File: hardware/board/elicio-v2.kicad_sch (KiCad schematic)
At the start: 65 parts, among them J1 TYPE-C-31-M-14, J2 SM02B-SRSS-TB, J3 HDR-3-RA, J4 TC2030-NL, P1 SIG1, P2 SIG2, P3 REF, Q1 AO3401A, Q2 2N7002, Q3 2N7002, Q4 2N7002, Q5 2N7002, SW1 4.5x4.5x1.6, U1 MDBT50Q-1MV2, U2 ADS1292IRSMT, U3 BQ25100YFPR, U4 TLV71330PDBVR, U5 USBLC6-2SC6

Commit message: board(v2): flex layout for interface II from WP11 winner
WP11 closed interface I at 0 runs, so the board is the 2-layer flex with ring-pad tabs on A_501015_series_w20.

Co-authored-by: Cursor <cursoragent@cursor.com>
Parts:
- P1, P2, P3: footprint elicio:PAD_8x8_ENIG -> elicio:RING_PAD_D5_H2.7
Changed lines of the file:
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@@
 		(date "2026-09-17")
 		(rev "0")
-		(comment 1 "WP12 board v2. Provisional 17 x 33 mm outline. Not for order.")
+		(comment 1 "WP12 board v2. Interface II flex, packing A_501015_series_w20. Schematic contract unchanged. Not for order.")
 	)
 	(symbol
@@
 			)
 		)
-		(property "Footprint" "elicio:PAD_8x8_ENIG"
+		(property "Footprint" "elicio:RING_PAD_D5_H2.7"
 			(at 254.0 50.8 0)
 			(show_name no)
@@
 			)
 		)
-		(property "Footprint" "elicio:PAD_8x8_ENIG"
+		(property "Footprint" "elicio:RING_PAD_D5_H2.7"
 			(at 254.0 76.2 0)
 			(show_name no)
@@
 			)
 		)
-		(property "Footprint" "elicio:PAD_8x8_ENIG"
+		(property "Footprint" "elicio:RING_PAD_D5_H2.7"
 			(at 254.0 101.6 0)
 			(show_name no)

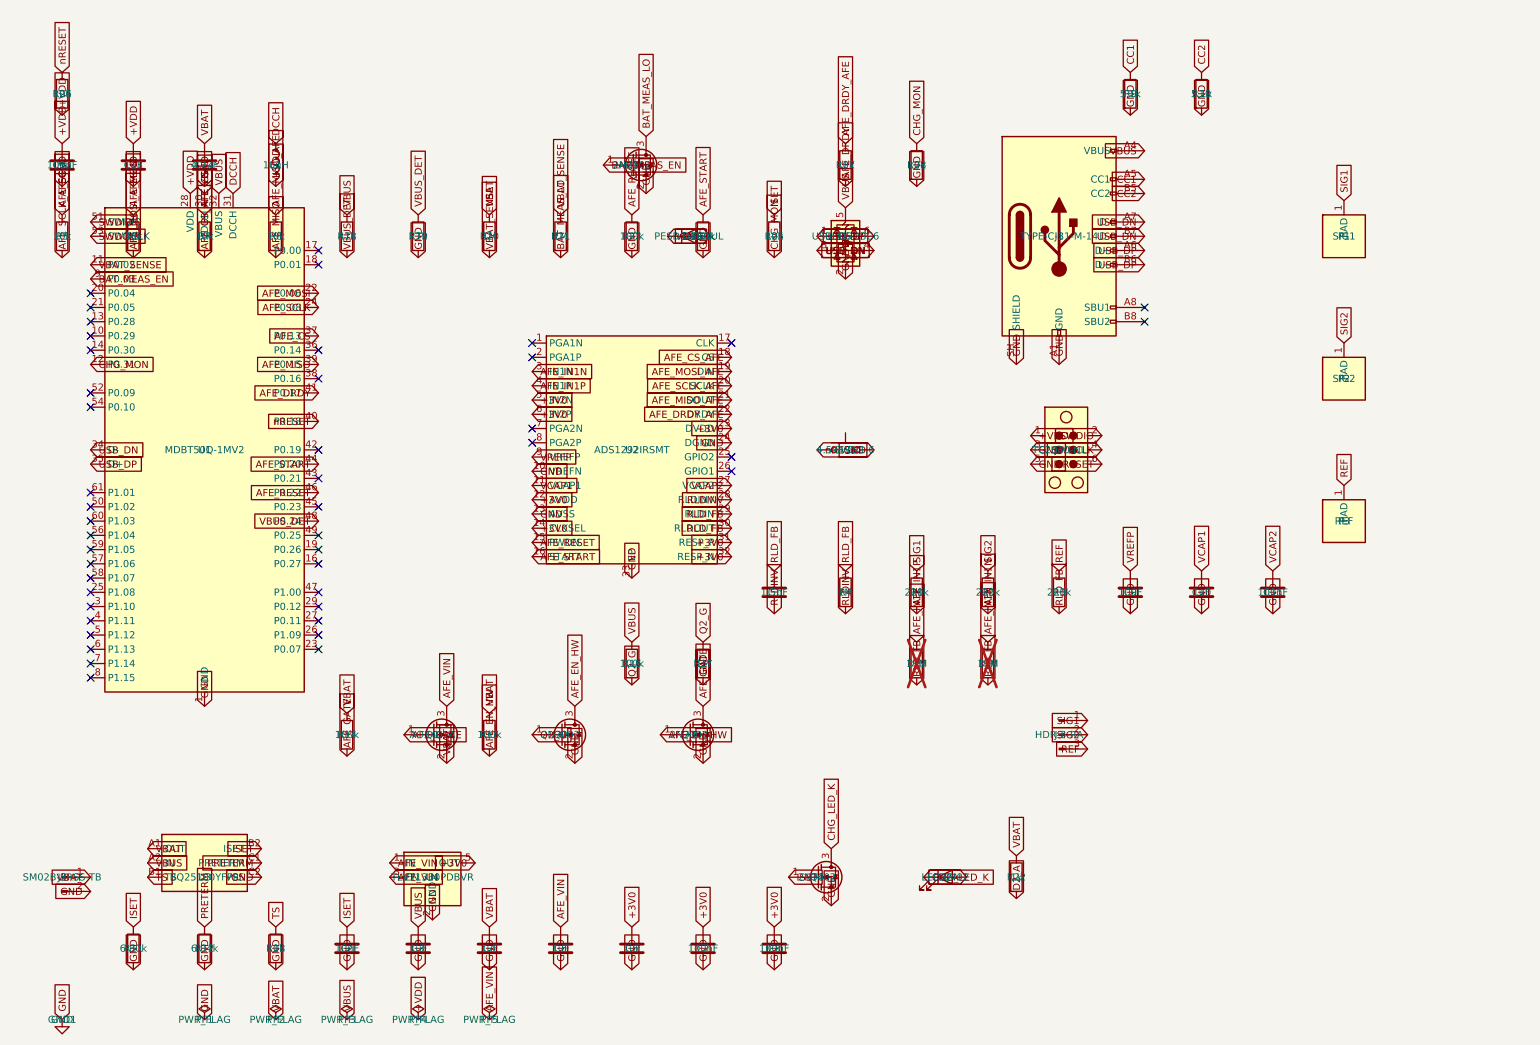
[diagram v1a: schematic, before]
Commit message: review(WP12): ISET, LED, divider, ERC 0/0, RF keep-out, routed flag, record
- ISET: R25 + R28 (20 k to GND) sat in parallel with RISET 6.80 k, so
  IOUT was about 26.6 mA, not 19.85. R28 now pulls LED_EN down; R25 alone
  feeds the high-impedance AIN7.
- LED: Q4's gate moves from ISET (about 1 V) to LED_EN (P0.04, pin 20);
  anode from VBUS, not VBAT, so it no longer loads the charger output.
- Battery divider: R21 to GND, Q5 DNP. The low-side switch left P0.02 at
  VBAT through 1 MΩ when off, above VDD + 0.3.
- ERC 0 errors, 0 warnings: mismatched symbols moved into lib/elicio as
  their embedded copies (netlist unchanged); J3 footprint library name.
- PCB: removed the length-along-s RF rule area that covered 15 module
  pads; the u-end area stays. Q5 DNP. Stiffener note 0.4.
- LCSC: C25803, C25765 and C1525 were each on two values (R1-R3 220 k
  among them); those 18 lines are blank, UNVERIFIED, for G3.
- release.py: summary has routed, tracks, nets and pads without a net;
  --routed fails closed on DRC errors, unconnected items, netless pads or
  no tracks. STEP with models. Tests cover both.
- board-v2.md: G2 default-state sentence, ESD actually used, REGOUT0 and
  the probe at a 1.8/3.0 V target, standoff stack 4.81 (no nut), foam 0.5,
  I = 0/720, decoupling deviates, DRC truth (PCB not synced, not placed).

Co-Authored-By: Claude Opus 5 <noreply@anthropic.com>
Claude-Session: https://claude.ai/code/session_014BkJUsEH26eSo9ULozTgDM
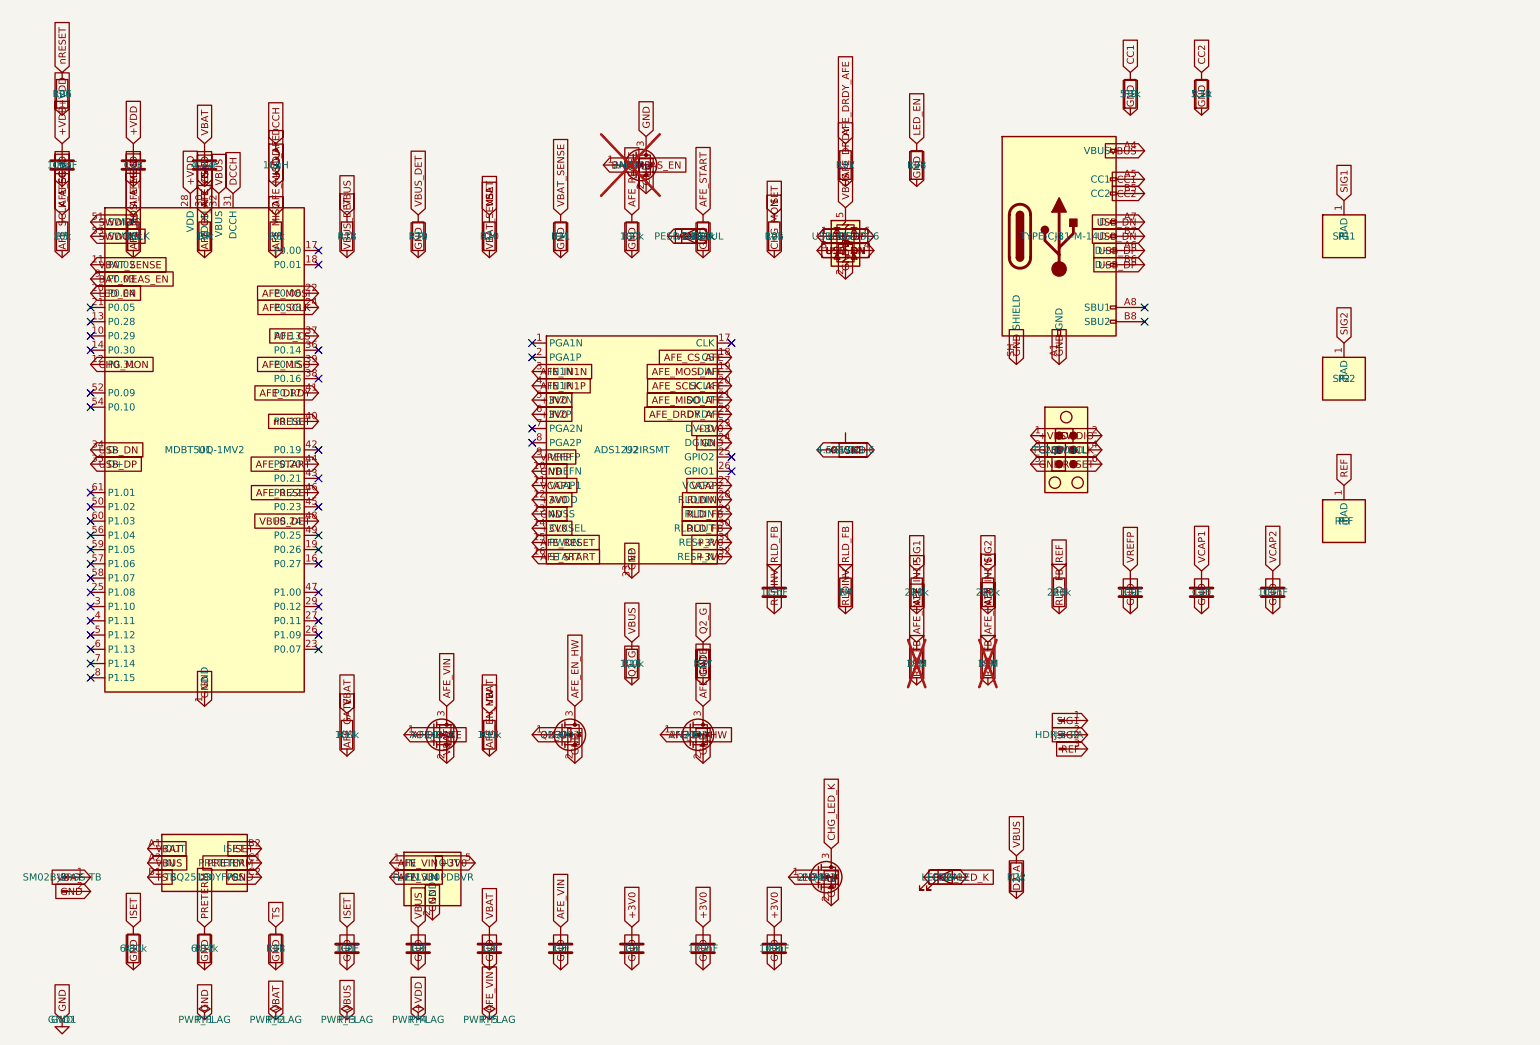
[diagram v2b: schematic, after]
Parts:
- C11, C12, C2, C7, C8: LCSC C1525 -> (none)
- D1: symbol Diode:PESD5V0L1UL -> elicio:PESD5V0L1UL
- J3: footprint Connector_PinHeader_2.54:PinHeader_1x03_P2.54mm_Horizontal -> Connector_PinHeader_2.54mm:PinHeader_1x03_P2.54mm_Horizontal
- Q1: symbol Transistor_FET:AO3401A -> elicio:AO3401A
- Q2, Q3, Q4: symbol Transistor_FET:2N7002 -> elicio:2N7002
- Q5: symbol Transistor_FET:2N7002 -> elicio:2N7002; now not fitted
- R1, R14, R15, R16, R2, R23, R24, R3: LCSC C25803 -> (none)
- R17, R20, R21, R22, R4: LCSC C25765 -> (none)
- U4: symbol Regulator_Linear:TLV71330PDBV -> elicio:TLV71330PDBV
- U5: symbol Power_Protection:USBLC6-2SC6 -> elicio:USBLC6-2SC6
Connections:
- net BAT_MEAS_LO is gone; now on net GND: Q5.3 (D), R21.2
- net CHG_MON: no longer R28.1
- net ISET: no longer Q4.1 (G)
- net VBAT: no longer R22.1
- net VBUS: now also R22.1
- net LED_EN: now reaches U1.20 (P0.04)
- net LED_EN: now also Q4.1 (G), R28.1
- no-connect marks 45 -> 44
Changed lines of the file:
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@@
 		(at 71.12 106.68)
 	)
-	(no_connect
-		(at 30.48 60.96)
+	(global_label "LED_EN"
+		(shape input)
+		(at 30.48 60.96 0)
+		(fields_autoplaced yes)
+		(effects
+			(font
+				(size 1.27 1.27)
+			)
+			(justify left)
+		)
 	)
 	(no_connect
@@
 	)
 	(symbol
-		(lib_id "Regulator_Linear:TLV71330PDBV")
+		(lib_id "elicio:TLV71330PDBV")
 		(at 91.44 165.1 0)
 		(unit 1)
@@
 			)
 		)
-		(property "Footprint" "Connector_PinHeader_2.54:PinHeader_1x03_P2.54mm_Horizontal"
+		(property "Footprint" "Connector_PinHeader_2.54mm:PinHeader_1x03_P2.54mm_Horizontal"
 			(at 203.2 139.7 0)
 			(show_name no)
@@
 	)
 	(symbol
-		(lib_id "Transistor_FET:AO3401A")
+		(lib_id "elicio:AO3401A")
 		(at 91.44 139.7 0)
 		(unit 1)
@@
 	)
 	(symbol
-		(lib_id "Transistor_FET:2N7002")
+		(lib_id "elicio:2N7002")
 		(at 114.3 139.7 0)
 		(unit 1)
@@
 	)
 	(symbol
-		(lib_id "Transistor_FET:2N7002")
+		(lib_id "elicio:2N7002")
 		(at 137.16 139.7 0)
 		(unit 1)
@@
 	)
 	(symbol
-		(lib_id "Transistor_FET:2N7002")
+		(lib_id "elicio:2N7002")
 		(at 160.02 165.1 0)
 		(unit 1)
@@
 		)
 	)
-	(global_label "ISET"
+	(global_label "LED_EN"
 		(shape input)
 		(at 154.94 165.1 0)
@@
 	)
 	(symbol
-		(lib_id "Power_Protection:USBLC6-2SC6")
+		(lib_id "elicio:USBLC6-2SC6")
 		(at 165.1 50.8 0)
 		(unit 1)
@@
 	)
 	(symbol
-		(lib_id "Diode:PESD5V0L1UL")
+		(lib_id "elicio:PESD5V0L1UL")
 		(at 137.16 50.8 0)
 		(unit 1)
@@
 			)
 		)
-		(property "LCSC" "C25803"
+		(property "LCSC" ""
 			(at 177.8 114.3 0)
 			(show_name no)
@@
 			)
 		)
-		(property "LCSC" "C25803"
+		(property "LCSC" ""
 			(at 190.5 114.3 0)
 			(show_name no)
@@
 			)
 		)
-		(property "LCSC" "C25803"
+		(property "LCSC" ""
 			(at 203.2 114.3 0)
 			(show_name no)
@@
 			)
 		)
-		(property "LCSC" "C25765"
+		(property "LCSC" ""
 			(at 165.1 114.3 0)
 			(show_name no)
@@
 			)
 		)
-		(property "LCSC" "C1525"
+		(property "LCSC" ""
 			(at 76.2 177.8 0)
 			(show_name no)
@@
 			)
 		)
-		(property "LCSC" "C25803"
+		(property "LCSC" ""
 			(at 76.2 139.7 0)
 			(show_name no)
@@
 			)
 		)
-		(property "LCSC" "C25803"
+		(property "LCSC" ""
 			(at 101.6 139.7 0)
 			(show_name no)
@@
 			)
 		)
-		(property "LCSC" "C25803"
+		(property "LCSC" ""
 			(at 127.0 127.0 0)
 			(show_name no)
@@
 			)
 		)
-		(property "LCSC" "C25765"
+		(property "LCSC" ""
 			(at 139.7 127.0 0)
 			(show_name no)
@@
 			)
 		)
-		(property "LCSC" "C25765"
+		(property "LCSC" ""
 			(at 101.6 50.8 0)
 			(show_name no)
@@
 			)
 		)
-		(property "LCSC" "C25765"
+		(property "LCSC" ""
 			(at 114.3 50.8 0)
 			(show_name no)
@@
 		)
 	)
-	(global_label "BAT_MEAS_LO"
+	(global_label "GND"
 		(shape input)
 		(at 114.3 54.61 90)
@@
 			)
 		)
-		(property "LCSC" "C1525"
+		(property "LCSC" ""
 			(at 139.7 177.8 0)
 			(show_name no)
@@
 			)
 		)
-		(property "LCSC" "C1525"
+		(property "LCSC" ""
 			(at 152.4 177.8 0)
 			(show_name no)
@@
 			)
 		)
-		(property "LCSC" "C1525"
+		(property "LCSC" ""
 			(at 241.3 114.3 0)
 			(show_name no)
@@
 			)
 		)
-		(property "LCSC" "C1525"
+		(property "LCSC" ""
 			(at 25.4 38.1 0)
 			(show_name no)
@@
 			)
 		)
-		(property "LCSC" "C25765"
+		(property "LCSC" ""
 			(at 195.58 165.1 0)
 			(show_name no)
@@
 		)
 	)
-	(global_label "VBAT"
+	(global_label "VBUS"
 		(shape input)
 		(at 195.58 161.29 270)
@@
 			)
 		)
-		(property "LCSC" "C25803"
+		(property "LCSC" ""
 			(at 127.0 50.8 0)
 			(show_name no)
@@
 			)
 		)
-		(property "LCSC" "C25803"
+		(property "LCSC" ""
 			(at 139.7 50.8 0)
 			(show_name no)
@@
 		)
 	)
-	(global_label "CHG_MON"
+	(global_label "LED_EN"
 		(shape input)
 		(at 177.8 34.29 270)
@@
 	)
 	(symbol
-		(lib_id "Transistor_FET:2N7002")
+		(lib_id "elicio:2N7002")
 		(at 127.0 38.1 0)
 		(unit 1)
@@
 		(on_board yes)
 		(in_pos_files yes)
-		(dnp no)
+		(dnp yes)
 		(property "Reference" "Q5"
 			(at 127.0 38.1 0)
@@
 		)
 	)
-	(global_label "BAT_MEAS_LO"
+	(global_label "GND"
 		(shape input)
 		(at 129.54 33.02 270)

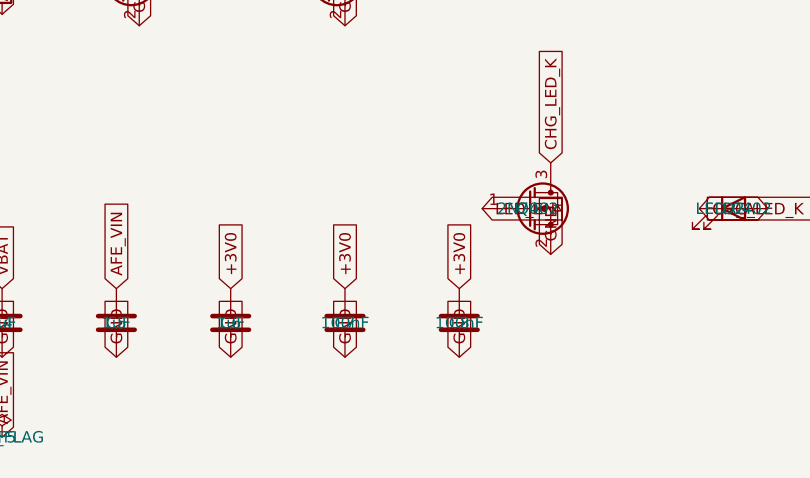
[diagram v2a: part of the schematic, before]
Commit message: fix(board-v2): Q68 ADS decoupling and LCSC fills
Co-authored-by: Cursor <cursoragent@cursor.com>
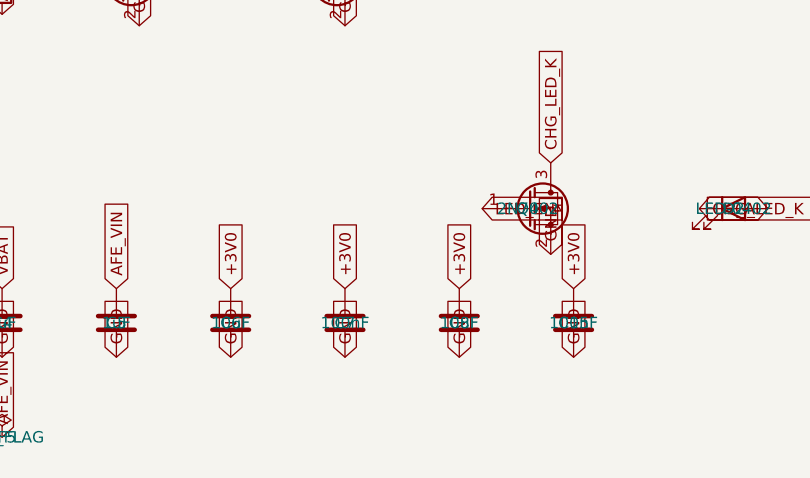
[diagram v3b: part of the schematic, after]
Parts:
- added C15: 100nF, Capacitor_SMD:C_0603_1608Metric, symbol Device:C
- C11, C12: LCSC (none) -> C1525
- C2: LCSC (none) -> C91601
- C6: value 1uF -> 10uF; footprint Capacitor_SMD:C_0402_1005Metric -> Capacitor_SMD:C_0603_1608Metric; LCSC C15849 -> C19702
- C7: footprint Capacitor_SMD:C_0402_1005Metric -> Capacitor_SMD:C_0603_1608Metric; LCSC (none) -> C14663
- C8: value 100nF -> 10uF; footprint Capacitor_SMD:C_0402_1005Metric -> Capacitor_SMD:C_0603_1608Metric; LCSC (none) -> C19702
- C9: LCSC C15850 -> C19702
- R1, R2, R3: LCSC (none) -> C881401
- R14, R15, R16, R23, R24: LCSC (none) -> C25741
- R17, R20, R21, R4: LCSC (none) -> C2782127
- R22: LCSC (none) -> C11702
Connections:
- net +3V0: now also C15.1
- net GND: now also C15.2
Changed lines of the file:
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@@
 			)
 		)
-		(property "LCSC" ""
+		(property "LCSC" "C881401"
 			(at 177.8 114.3 0)
 			(show_name no)
@@
 			)
 		)
-		(property "LCSC" ""
+		(property "LCSC" "C881401"
 			(at 190.5 114.3 0)
 			(show_name no)
@@
 			)
 		)
-		(property "LCSC" ""
+		(property "LCSC" "C881401"
 			(at 203.2 114.3 0)
 			(show_name no)
@@
 			)
 		)
-		(property "LCSC" ""
+		(property "LCSC" "C2782127"
 			(at 165.1 114.3 0)
 			(show_name no)
@@
 			)
 		)
-		(property "LCSC" ""
+		(property "LCSC" "C91601"
 			(at 76.2 177.8 0)
 			(show_name no)
@@
 			)
 		)
-		(property "LCSC" ""
+		(property "LCSC" "C25741"
 			(at 76.2 139.7 0)
 			(show_name no)
@@
 			)
 		)
-		(property "LCSC" ""
+		(property "LCSC" "C25741"
 			(at 101.6 139.7 0)
 			(show_name no)
@@
 			)
 		)
-		(property "LCSC" ""
+		(property "LCSC" "C25741"
 			(at 127.0 127.0 0)
 			(show_name no)
@@
 			)
 		)
-		(property "LCSC" ""
+		(property "LCSC" "C2782127"
 			(at 139.7 127.0 0)
 			(show_name no)
@@
 			)
 		)
-		(property "LCSC" ""
+		(property "LCSC" "C2782127"
 			(at 101.6 50.8 0)
 			(show_name no)
@@
 			)
 		)
-		(property "LCSC" ""
+		(property "LCSC" "C2782127"
 			(at 114.3 50.8 0)
 			(show_name no)
@@
 			)
 		)
-		(property "Value" "1uF"
+		(property "Value" "10uF"
 			(at 127.0 177.8 0)
 			(show_name no)
@@
 			)
 		)
-		(property "Footprint" "Capacitor_SMD:C_0402_1005Metric"
+		(property "Footprint" "Capacitor_SMD:C_0603_1608Metric"
 			(at 127.0 177.8 0)
 			(show_name no)
@@
 			)
 		)
-		(property "LCSC" "C15849"
+		(property "LCSC" "C19702"
 			(at 127.0 177.8 0)
 			(show_name no)
@@
 			)
 		)
-		(property "Footprint" "Capacitor_SMD:C_0402_1005Metric"
+		(property "Footprint" "Capacitor_SMD:C_0603_1608Metric"
 			(at 139.7 177.8 0)
 			(show_name no)
@@
 			)
 		)
-		(property "LCSC" ""
+		(property "LCSC" "C14663"
 			(at 139.7 177.8 0)
 			(show_name no)
@@
 			)
 		)
-		(property "Value" "100nF"
+		(property "Value" "10uF"
 			(at 152.4 177.8 0)
 			(show_name no)
@@
 			)
 		)
-		(property "Footprint" "Capacitor_SMD:C_0402_1005Metric"
+		(property "Footprint" "Capacitor_SMD:C_0603_1608Metric"
 			(at 152.4 177.8 0)
 			(show_name no)
@@
 			)
 		)
-		(property "LCSC" ""
+		(property "LCSC" "C19702"
 			(at 152.4 177.8 0)
 			(show_name no)
@@
 	(symbol
 		(lib_id "Device:C")
+		(at 165.1 177.8 0)
+		(unit 1)
+		(body_style 1)
+		(exclude_from_sim no)
+		(in_bom yes)
+		(on_board yes)
+		(in_pos_files yes)
+		(dnp no)
+		(property "Reference" "C15"
+			(at 165.1 177.8 0)
+			(show_name no)
+			(do_not_autoplace no)
+			(effects
+				(font
+					(size 1.27 1.27)
+				)
+			)
+		)
+		(property "Value" "100nF"
+			(at 165.1 177.8 0)
+			(show_name no)
+			(do_not_autoplace no)
+			(effects
+				(font
+					(size 1.27 1.27)
+				)
+			)
+		)
+		(property "Footprint" "Capacitor_SMD:C_0603_1608Metric"
+			(at 165.1 177.8 0)
+			(show_name no)
+			(do_not_autoplace no)
+			(hide yes)
+			(effects
+				(font
+					(size 1.27 1.27)
+				)
+			)
+		)
+		(property "Datasheet" "~"
+			(at 165.1 177.8 0)
+			(show_name no)
+			(do_not_autoplace no)
+			(hide yes)
+			(effects
+				(font
+					(size 1.27 1.27)
+				)
+			)
+		)
+		(property "LCSC" "C14663"
+			(at 165.1 177.8 0)
+			(show_name no)
+			(do_not_autoplace no)
+			(hide yes)
+			(effects
+				(font
+					(size 1.27 1.27)
+				)
+			)
+		)
+		(pin "1"
+		)
+		(pin "2"
+		)
+		(instances
+			(project "elicio-v2"
+				(path "/420b5650-2bf7-4a1a-b8d9-f0e848e2539f"
+					(reference "C15")
+					(unit 1)
+				)
+			)
+		)
+	)
+	(global_label "+3V0"
+		(shape input)
+		(at 165.1 173.99 270)
+		(fields_autoplaced yes)
+		(effects
+			(font
+				(size 1.27 1.27)
+			)
+			(justify left)
+		)
+	)
+	(global_label "GND"
+		(shape input)
+		(at 165.1 181.61 90)
+		(fields_autoplaced yes)
+		(effects
+			(font
+				(size 1.27 1.27)
+			)
+			(justify left)
+		)
+	)
+	(symbol
+		(lib_id "Device:C")
 		(at 215.9 114.3 0)
 		(unit 1)
@@
 			)
 		)
-		(property "LCSC" "C15850"
+		(property "LCSC" "C19702"
 			(at 215.9 114.3 0)
 			(show_name no)
@@
 			)
 		)
-		(property "LCSC" ""
+		(property "LCSC" "C1525"
 			(at 241.3 114.3 0)
 			(show_name no)
@@
 			)
 		)
-		(property "LCSC" ""
+		(property "LCSC" "C1525"
 			(at 25.4 38.1 0)
 			(show_name no)
@@
 			)
 		)
-		(property "LCSC" ""
+		(property "LCSC" "C11702"
 			(at 195.58 165.1 0)
 			(show_name no)
@@
 			)
 		)
-		(property "LCSC" ""
+		(property "LCSC" "C25741"
 			(at 127.0 50.8 0)
 			(show_name no)
@@
 			)
 		)
-		(property "LCSC" ""
+		(property "LCSC" "C25741"
 			(at 139.7 50.8 0)
 			(show_name no)
